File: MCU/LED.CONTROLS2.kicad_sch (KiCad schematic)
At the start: 22 parts, among them U3 HHG1D-1, U4 AMC1301DWVR, U6 LM5012DDAR

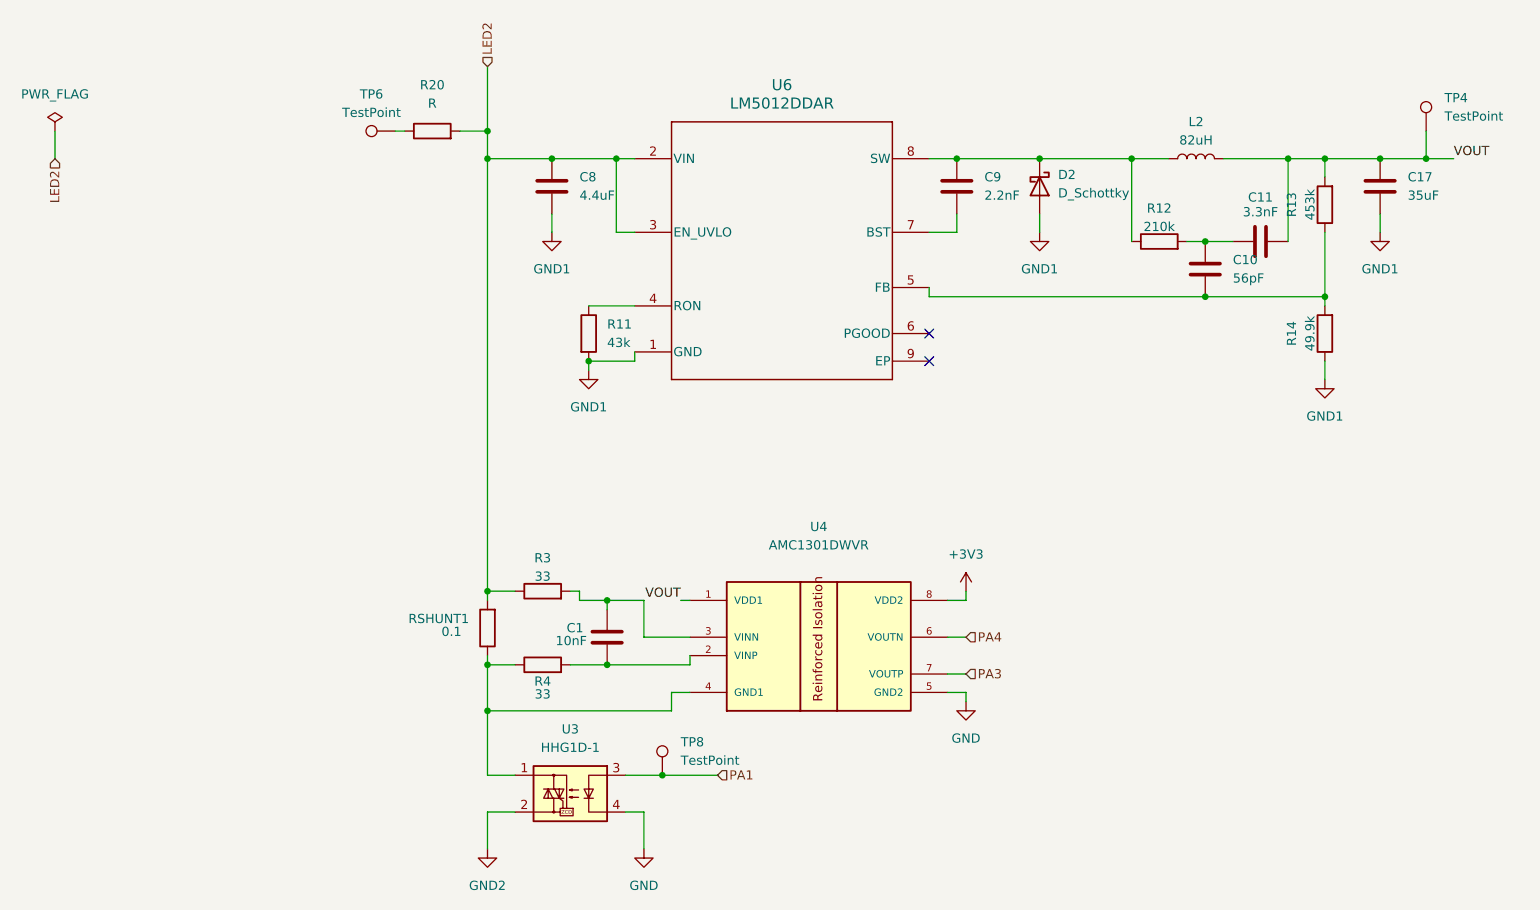
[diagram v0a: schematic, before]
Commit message: Centralized isolation amp power source. Corrected STM32 pins.
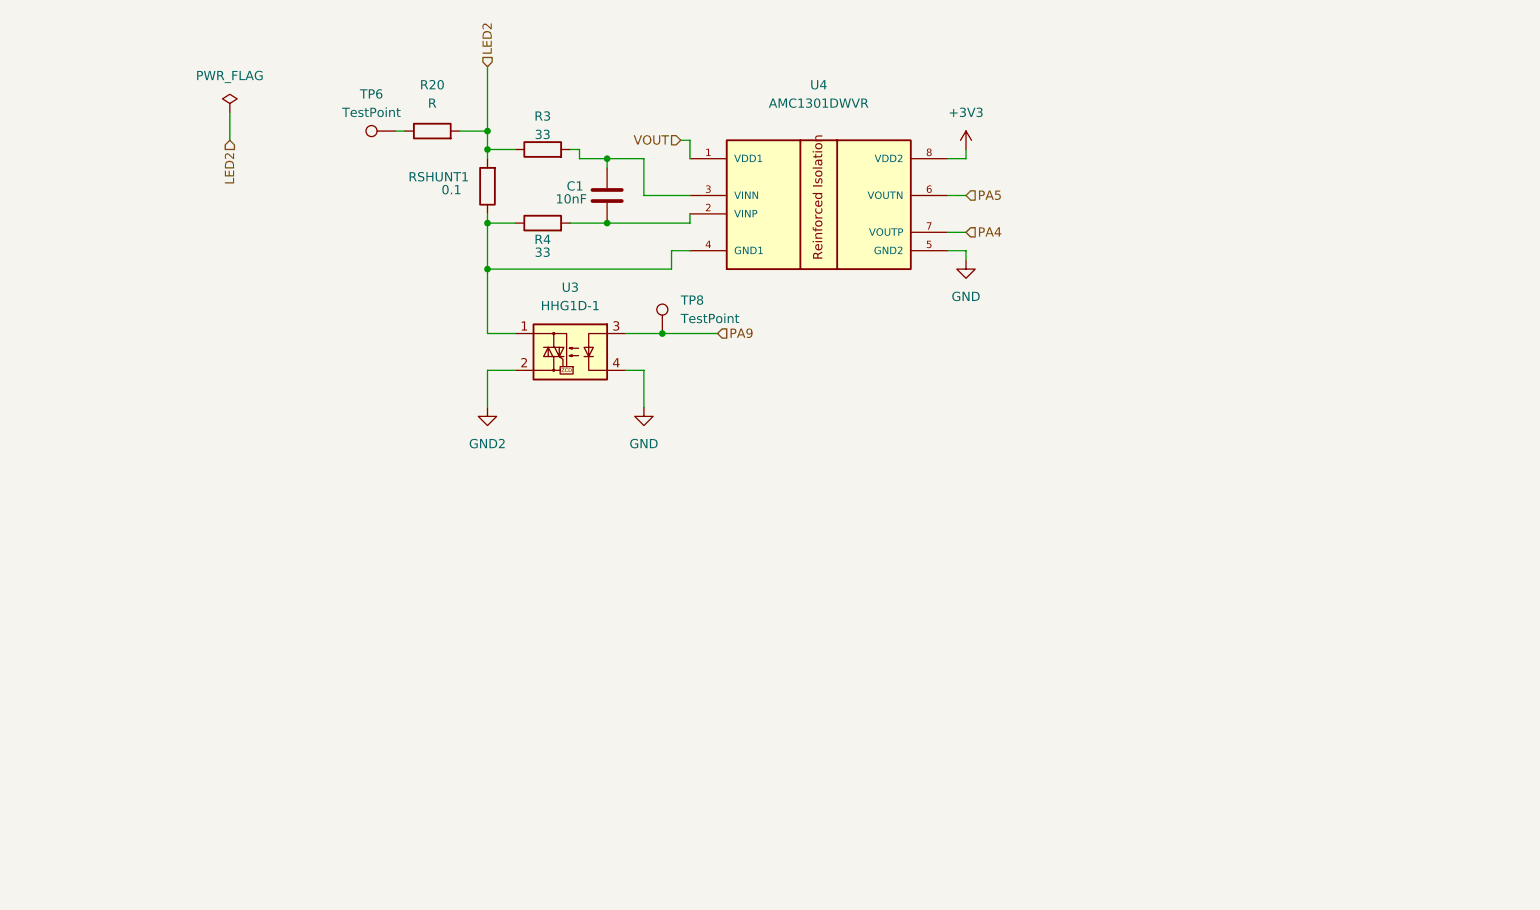
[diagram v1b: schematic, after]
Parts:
- removed C10: 56pF, symbol Device:C
- removed C11: 3.3nF, symbol Device:C
- removed C17: 35uF, symbol Device:C
- removed C8: 4.4uF, symbol Device:C
- removed C9: 2.2nF, symbol Device:C
- removed D2: D_Schottky, symbol Device:D_Schottky
- removed L2: 82uH, symbol Device:L
- removed R11: 43k, symbol Device:R
- removed R12: 210k, Resistor_SMD:R_1812_4532Metric_Pad1.30x3.40mm_HandSolder, symbol Device:R
- removed R13: 453k, Resistor_SMD:R_1812_4532Metric_Pad1.30x3.40mm_HandSolder, symbol Device:R
- removed R14: 49.9k, Resistor_SMD:R_1812_4532Metric_Pad1.30x3.40mm_HandSolder, symbol Device:R
- removed TP4: TestPoint, symbol Connector:TestPoint
- removed U6: LM5012DDAR, DDA0008E-IPC_A, symbol LM 5012 Buck Converter:LM5012DDAR
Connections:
- net PA3 is gone; now on net PA4: U4.7 (VOUTP)
- net PA4: no longer U4.6 (VOUTN)
- net PA1 renamed PA9
- new net PA5: U4.6 (VOUTN)
- no-connect marks 2 -> 0
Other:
- moved on the sheet: C1, R3, R4, RSHUNT1, TP8, U3, U4

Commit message: Assigned footprints and added RTD
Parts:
- removed R20: R, symbol Device:R
- removed RSHUNT1: 0.1, Resistor_SMD:R_1812_4532Metric_Pad1.30x3.40mm_HandSolder, symbol Device:R
- added RSHUNT2: 0.1, Resistor_SMD:R_1812_4532Metric_Pad1.30x3.40mm_HandSolder, symbol Device:R
- C1: footprint (none) -> Capacitor_SMD:C_1206_3216Metric
- TP6: value TestPoint -> Post_LED2_Test; footprint (none) -> TestPoint:TestPoint_Pad_2.0x2.0mm
- TP8: value TestPoint -> LED2_MCU_CT; footprint (none) -> TestPoint:TestPoint_Pad_1.5x1.5mm
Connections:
- net LED2: now also TP6.1, RSHUNT2.2
- net at R4.1, U3.1, U4.4 (GND1): now also RSHUNT2.1
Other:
- moved on the sheet: TP6
